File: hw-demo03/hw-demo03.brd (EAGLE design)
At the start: 83.5 x 63.5 mm, 41 parts, among them IC3 MCP2562T, IC4 STM32F042

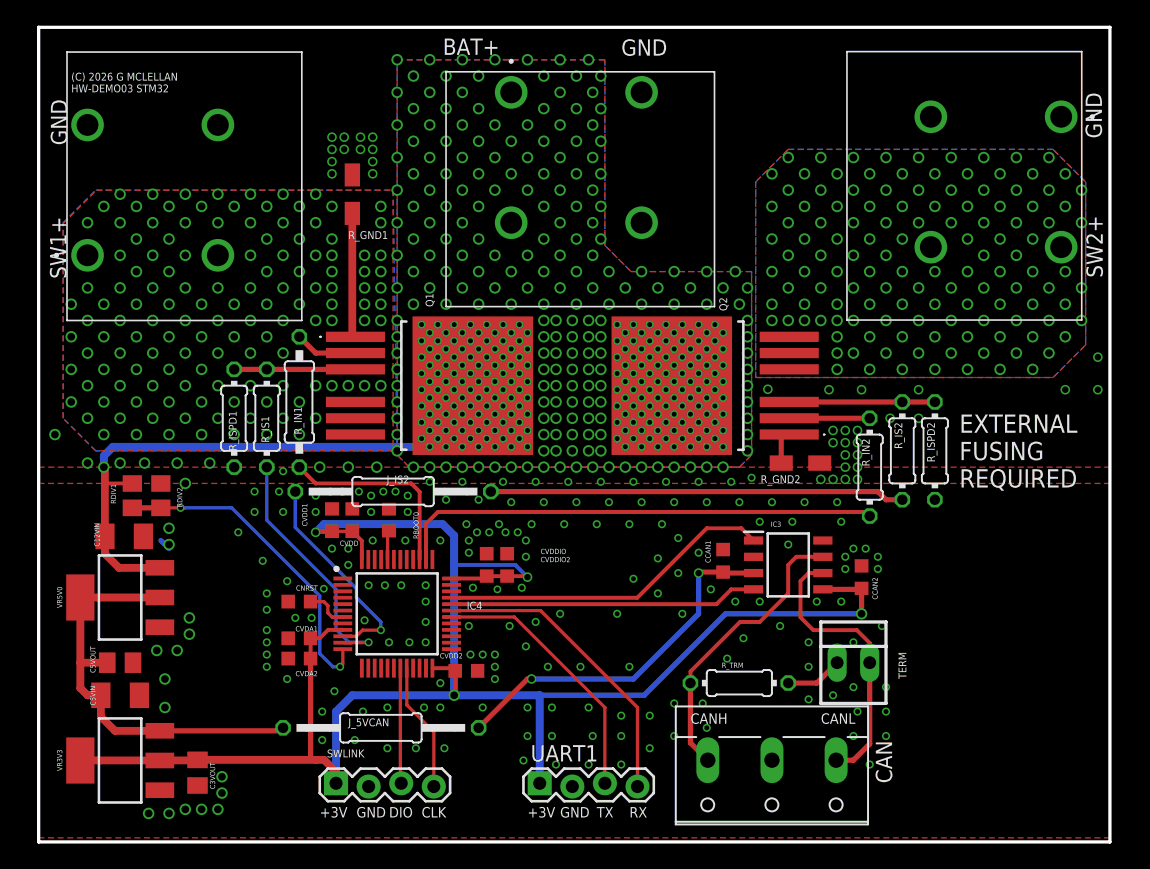
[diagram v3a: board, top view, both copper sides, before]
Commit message: add cap on voltage divider, more stitching
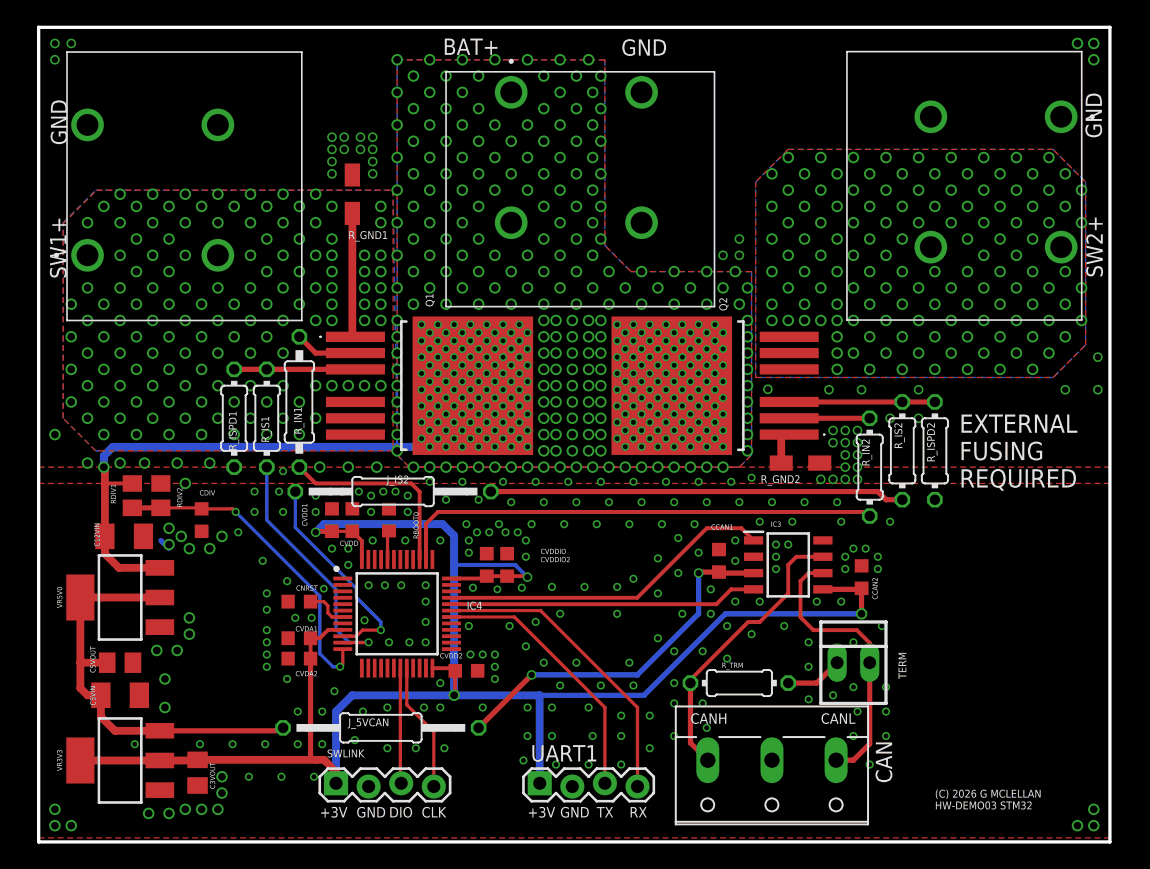
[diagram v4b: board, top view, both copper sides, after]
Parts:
- added CDIV: 100n, rcl:C0603K
- moved CCAN1 0.32 mm to (54.3, 21.9)
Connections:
- net ADC2: now also CDIV.1
- net GND: now also CDIV.2, IC3.8
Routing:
- net GND: vias 230 -> 277
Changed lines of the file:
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@@
 <text x="52.07" y="9.2075" size="0.8128" layer="25" font="vector" ratio="14">CANH</text>
 <text x="3.4925" y="54.2925" size="1.27" layer="25" font="vector" ratio="14" rot="R90">GND</text>
-<text x="3.81" y="58.42" size="0.6096" layer="25" font="vector" ratio="14">(C) 2026 G MCLELLAN
+<text x="71.12" y="2.54" size="0.6096" layer="25" font="vector" ratio="14">(C) 2026 G MCLELLAN
 HW-DEMO03 STM32</text>
 <text x="46.6725" y="61.2775" size="1.27" layer="25" font="vector" ratio="14">GND</text>
@@
 <attribute name="NAME" x="66.5153" y="7.9083" size="1.27" layer="25" font="vector" ratio="14" rot="R270"/>
 </element>
-<element name="CCAN1" library="rcl" package="C0603K" value="100n" x="54.61" y="21.9075" smashed="yes" rot="R90">
-<attribute name="NAME" x="53.6425" y="21.7425" size="0.4064" layer="25" font="vector" ratio="14" rot="R90"/>
+<element name="CCAN1" library="rcl" package="C0603K" value="100n" x="54.2925" y="21.9075" smashed="yes" rot="R90">
+<attribute name="NAME" x="55.41" y="24.75" size="0.4064" layer="25" font="vector" ratio="14" rot="R180"/>
 </element>
 <element name="CCAN2" library="rcl" package="C0603K" value="100n" x="65.405" y="20.6375" smashed="yes" rot="R90">
@@
 <element name="J_5VCAN" library="rcl" package="0207/15" value="000" x="27.94" y="8.89" smashed="yes" rot="R180">
 <attribute name="NAME" x="25.4" y="9.017" size="0.6096" layer="25" font="vector" ratio="14"/>
+</element>
+<element name="CDIV" library="rcl" package="C0603K" value="100n" x="13.97" y="25.0825" smashed="yes" rot="R270">
+<attribute name="NAME" x="13.805" y="27.0025" size="0.4064" layer="25" ratio="14"/>
 </element>
 </elements>
@@
 <contactref element="UART1" pad="2"/>
 <via x="32.5755" y="23.495" extent="1-16" drill="0.381"/>
-<via x="40.9575" y="13.6525" extent="1-16" drill="0.381"/>
+<via x="40.64" y="13.97" extent="1-16" drill="0.381"/>
 <via x="34.925" y="14.605" extent="1-16" drill="0.381"/>
 <via x="52.705" y="22.5425" extent="1-16" drill="0.381"/>
@@
 <via x="47.625" y="20.5105" extent="1-16" drill="0.381"/>
 <contactref element="SWLINK" pad="2"/>
-<via x="43.4975" y="13.6525" extent="1-16" drill="0.381"/>
+<via x="43.18" y="13.97" extent="1-16" drill="0.381"/>
 <via x="46.6725" y="6.0325" extent="1-16" drill="0.381"/>
-<via x="47.3075" y="13.6525" extent="1-16" drill="0.381"/>
+<via x="47.3075" y="13.97" extent="1-16" drill="0.381"/>
 <via x="54.9275" y="14.2875" extent="1-16" drill="0.381"/>
 <contactref element="BAT+" pad="2_2"/>
@@
 <vertex x="1.27" y="0.3175"/>
 </polygon>
-<via x="59.055" y="16.8275" extent="1-16" drill="0.381"/>
-<via x="56.1975" y="15.875" extent="1-16" drill="0.381"/>
+<via x="59.3725" y="16.8275" extent="1-16" drill="0.381"/>
+<via x="56.8325" y="16.1925" extent="1-16" drill="0.381"/>
 <contactref element="C12VIN" pad="2"/>
 <contactref element="VR5V0" pad="1"/>
@@
 <via x="24.3205" y="11.7475" extent="1-16" drill="0.381"/>
 <via x="23.368" y="10.16" extent="1-16" drill="0.381"/>
-<via x="23.368" y="7.9375" extent="1-16" drill="0.381"/>
+<via x="23.368" y="7.62" extent="1-16" drill="0.381"/>
 <via x="25.908" y="7.9375" extent="1-16" drill="0.381"/>
 <via x="26.543" y="10.16" extent="1-16" drill="0.381"/>
+<via x="46.355" y="19.8755" extent="1-16" drill="0.381"/>
+<via x="43.815" y="19.8755" extent="1-16" drill="0.381"/>
+<via x="41.275" y="19.8755" extent="1-16" drill="0.381"/>
+<via x="52.3875" y="24.765" extent="1-16" drill="0.381"/>
+<via x="2.54" y="1.27" extent="1-16" drill="0.6"/>
+<via x="2.54" y="2.54" extent="1-16" drill="0.6"/>
+<via x="3.81" y="1.27" extent="1-16" drill="0.6"/>
+<via x="83.5025" y="1.27" extent="1-16" drill="0.6"/>
+<via x="82.2325" y="1.27" extent="1-16" drill="0.6"/>
+<via x="83.5025" y="2.54" extent="1-16" drill="0.6"/>
+<via x="83.5025" y="62.23" extent="1-16" drill="0.6"/>
+<via x="83.5025" y="60.96" extent="1-16" drill="0.6"/>
+<via x="82.2325" y="62.23" extent="1-16" drill="0.6"/>
+<via x="3.81" y="62.23" extent="1-16" drill="0.5"/>
+<contactref element="CDIV" pad="2"/>
+<via x="12.3825" y="23.8125" extent="1-16" drill="0.6"/>
+<via x="15.5575" y="23.8125" extent="1-16" drill="0.6"/>
+<via x="13.0175" y="22.86" extent="1-16" drill="0.6"/>
+<via x="14.605" y="22.86" extent="1-16" drill="0.6"/>
+<via x="2.54" y="62.23" extent="1-16" drill="0.5"/>
+<via x="2.54" y="60.96" extent="1-16" drill="0.5"/>
+<via x="21.463" y="7.62" extent="1-16" drill="0.381"/>
+<via x="18.923" y="7.62" extent="1-16" drill="0.381"/>
+<via x="16.383" y="7.62" extent="1-16" drill="0.381"/>
+<via x="13.843" y="7.62" extent="1-16" drill="0.381"/>
+<via x="8.763" y="7.62" extent="1-16" drill="0.381"/>
+<via x="17.653" y="5.08" extent="1-16" drill="0.381"/>
+<via x="20.193" y="5.08" extent="1-16" drill="0.381"/>
+<via x="22.733" y="5.08" extent="1-16" drill="0.381"/>
+<via x="21.463" y="10.16" extent="1-16" drill="0.381"/>
+<via x="55.5625" y="21.9075" extent="1-16" drill="0.381"/>
+<via x="55.5625" y="23.495" extent="1-16" drill="0.381"/>
+<via x="58.7375" y="22.225" extent="1-16" drill="0.381"/>
+<via x="58.7375" y="23.1775" extent="1-16" drill="0.381"/>
+<via x="58.7375" y="21.2725" extent="1-16" drill="0.381"/>
+<contactref element="IC3" pad="8"/>
+<via x="55.88" y="45.72" extent="1-16" drill="0.5"/>
+<via x="55.88" y="46.99" extent="1-16" drill="0.5"/>
+<via x="54.61" y="45.72" extent="1-16" drill="0.5"/>
+<via x="67.6275" y="24.9555" extent="1-16" drill="0.381"/>
+<via x="41.91" y="12.192" extent="1-16" drill="0.381"/>
+<via x="45.085" y="12.192" extent="1-16" drill="0.381"/>
+<via x="47.625" y="12.192" extent="1-16" drill="0.381"/>
+<via x="53.6575" y="17.78" extent="1-16" drill="0.381"/>
+<via x="49.53" y="15.875" extent="1-16" drill="0.381"/>
+<via x="50.8" y="12.3825" extent="1-16" drill="0.381"/>
+<via x="54.9275" y="16.8275" extent="1-16" drill="0.381"/>
+<via x="50.8" y="14.859" extent="1-16" drill="0.381"/>
+<via x="53.0225" y="14.859" extent="1-16" drill="0.381"/>
 </signal>
 <signal name="CANH">
@@
 <wire x1="59.69" y1="21.59" x2="59.69" y2="19.3675" width="0.3048" layer="1"/>
 <wire x1="59.69" y1="19.3675" x2="57.4675" y2="17.145" width="0.3048" layer="1"/>
-<wire x1="57.4675" y1="17.145" x2="55.932553125" y2="17.145" width="0.3048" layer="1"/>
-<wire x1="55.932553125" y1="17.145" x2="52.07" y2="13.282446875" width="0.3048" layer="1"/>
-<wire x1="52.07" y1="13.282446875" x2="52.07" y2="12.3825" width="0.3048" layer="1"/>
+<wire x1="57.4675" y1="17.145" x2="56.567553125" y2="17.145" width="0.3048" layer="1"/>
+<wire x1="56.567553125" y1="17.145" x2="52.07" y2="12.647446875" width="0.3048" layer="1"/>
+<wire x1="52.07" y1="12.647446875" x2="52.07" y2="12.3825" width="0.3048" layer="1"/>
 <wire x1="53.42" y1="6.37" x2="52.07" y2="7.72" width="0.4064" layer="1"/>
 <wire x1="52.07" y1="7.72" x2="52.07" y2="12.3825" width="0.4064" layer="1"/>
@@
 <wire x1="24.765" y1="13.6525" x2="24.972" y2="13.8595" width="0.254" layer="1"/>
 <wire x1="24.972" y1="13.8595" x2="24.972" y2="15.03" width="0.254" layer="1"/>
-<wire x1="10.795" y1="26.0375" x2="12.33146875" y2="26.0375" width="0.254" layer="1"/>
-<via x="12.33146875" y="26.0375" extent="1-16" drill="0.381"/>
-<wire x1="12.33146875" y1="26.0375" x2="12.677753125" y2="26.0375" width="0.254" layer="16"/>
 <wire x1="23.1775" y1="14.67995" x2="23.1775" y2="19.172146875" width="0.254" layer="16"/>
-<wire x1="23.1775" y1="19.172146875" x2="16.312146875" y2="26.0375" width="0.254" layer="16"/>
-<wire x1="16.312146875" y1="26.0375" x2="12.33146875" y2="26.0375" width="0.254" layer="16"/>
+<wire x1="23.1775" y1="19.172146875" x2="16.629646875" y2="25.72" width="0.254" layer="16"/>
+<contactref element="CDIV" pad="1"/>
+<wire x1="10.795" y1="26.0375" x2="13.97" y2="26.0375" width="0.254" layer="1"/>
+<wire x1="13.97" y1="26.0375" x2="13.97" y2="25.9575" width="0.254" layer="1"/>
+<wire x1="13.97" y1="25.9575" x2="16.392146875" y2="25.9575" width="0.254" layer="1"/>
+<wire x1="16.392146875" y1="25.9575" x2="16.629646875" y2="25.72" width="0.254" layer="1"/>
+<via x="16.629646875" y="25.72" extent="1-16" drill="0.381"/>
 </signal>
 <signal name="BOOT0">
@@
 <contactref element="Q2" pad="1"/>
 <contactref element="R_GND2" pad="2"/>
-<wire x1="59.1435" y1="29.5275" x2="59.1435" y2="31.75" width="0.4064" layer="1"/>
+<wire x1="59.1435" y1="29.5275" x2="59.1435" y2="31.75" width="0.6096" layer="1"/>
 <wire x1="59.1435" y1="31.75" x2="59.765" y2="31.75" width="0.4064" layer="1"/>
 </signal>
@@
 <contactref element="CCAN1" pad="1"/>
 <contactref element="J_5VCAN" pad="1"/>
-<wire x1="54.61" y1="21.0325" x2="52.705" y2="21.0325" width="0.4064" layer="1"/>
+<wire x1="54.2925" y1="21.0325" x2="52.705" y2="21.0325" width="0.4064" layer="1"/>
 <wire x1="52.705" y1="21.0325" x2="52.705" y2="20.955" width="0.4064" layer="1"/>
 <via x="52.705" y="20.955" extent="1-16" drill="0.5"/>
 <wire x1="52.705" y1="20.955" x2="52.705" y2="17.78" width="0.4064" layer="16"/>
-<wire x1="52.705" y1="17.78" x2="47.625" y2="12.7" width="0.4064" layer="16"/>
-<wire x1="47.625" y1="12.7" x2="39.6875" y2="12.7" width="0.4064" layer="16"/>
-<wire x1="35.56" y1="8.89" x2="39.37" y2="12.7" width="0.4064" layer="1"/>
-<wire x1="39.37" y1="12.7" x2="39.6875" y2="12.7" width="0.4064" layer="1"/>
-<via x="39.6875" y="12.7" extent="1-16" drill="0.5"/>
+<wire x1="52.705" y1="17.78" x2="47.9425" y2="13.0175" width="0.4064" layer="16"/>
+<wire x1="47.9425" y1="13.0175" x2="39.6875" y2="13.0175" width="0.4064" layer="16"/>
+<wire x1="35.56" y1="8.89" x2="39.6875" y2="13.0175" width="0.4064" layer="1"/>
+<via x="39.6875" y="13.0175" extent="1-16" drill="0.5"/>
 <wire x1="56.99" y1="20.955" x2="54.6875" y2="20.955" width="0.4064" layer="1"/>
-<wire x1="54.6875" y1="20.955" x2="54.61" y2="21.0325" width="0.4064" layer="1"/>
+<wire x1="54.6875" y1="20.955" x2="54.2925" y2="21.0325" width="0.4064" layer="1"/>
 </signal>
 </signals>

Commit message: pretty happy with the layout
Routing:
- net GND: vias 277 -> 279
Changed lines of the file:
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@@
 </element>
 <element name="R_IN1" library="rcl" package="0207/10" value="4K7" x="21.59" y="34.29" smashed="yes" rot="R90">
-<attribute name="NAME" x="21.7805" y="31.75" size="0.6096" layer="25" font="vector" ratio="14" rot="R90"/>
+<attribute name="NAME" x="25.0825" y="30.988" size="0.6096" layer="25" font="vector" ratio="14" rot="R180"/>
 </element>
 <element name="BAT+" library="VP0265840000G" package="AMPHENOL_VP0265840000G" value="" x="43.18" y="53.34" smashed="yes">
@@
 </element>
 <element name="R_ISPD1" library="rcl" package="0204/7" value="1K0" x="16.51" y="33.02" smashed="yes" rot="R90">
-<attribute name="NAME" x="16.7005" y="30.48" size="0.6096" layer="25" ratio="10" rot="R90"/>
+<attribute name="NAME" x="17.78" y="30.988" size="0.6096" layer="25" ratio="10" rot="R180"/>
 </element>
 <element name="R_IS1" library="rcl" package="0204/7" value="10K" x="19.05" y="33.02" smashed="yes" rot="R270">
-<attribute name="NAME" x="19.2405" y="31.115" size="0.6096" layer="25" ratio="10" rot="R90"/>
+<attribute name="NAME" x="20.6375" y="30.988" size="0.6096" layer="25" ratio="10" rot="R180"/>
 </element>
 <element name="R_GND1" library="rcl" package="R1206W" value="0R0" x="25.7175" y="50.4825" smashed="yes" rot="R270">
@@
 <via x="16.8275" y="24.13" extent="1-16" drill="0.381"/>
 <via x="18.7325" y="21.9075" extent="1-16" drill="0.381"/>
-<via x="33.02" y="26.67" extent="1-16" drill="0.381"/>
 <via x="34.6075" y="24.765" extent="1-16" drill="0.381"/>
 <via x="37.1475" y="24.765" extent="1-16" drill="0.381"/>
@@
 <via x="47.3075" y="24.765" extent="1-16" drill="0.381"/>
 <via x="49.8475" y="24.765" extent="1-16" drill="0.381"/>
-<via x="35.56" y="26.67" extent="1-16" drill="0.381"/>
 <via x="38.1" y="26.4795" extent="1-16" drill="0.381"/>
 <via x="40.64" y="26.4795" extent="1-16" drill="0.381"/>
@@
 <via x="28.448" y="7.3025" extent="1-16" drill="0.381"/>
 <via x="28.448" y="10.4775" extent="1-16" drill="0.381"/>
-<via x="24.3205" y="11.7475" extent="1-16" drill="0.381"/>
+<via x="24.9555" y="12.065" extent="1-16" drill="0.381"/>
 <via x="23.368" y="10.16" extent="1-16" drill="0.381"/>
 <via x="23.368" y="7.62" extent="1-16" drill="0.381"/>
@@
 <via x="50.8" y="14.859" extent="1-16" drill="0.381"/>
 <via x="53.0225" y="14.859" extent="1-16" drill="0.381"/>
+<via x="35.56" y="26.4795" extent="1-16" drill="0.381"/>
+<via x="33.655" y="26.4795" extent="1-16" drill="0.381"/>
+<via x="31.75" y="26.4795" extent="1-16" drill="0.381"/>
+<via x="45.72" y="13.97" extent="1-16" drill="0.381"/>
 </signal>
 <signal name="CANH">

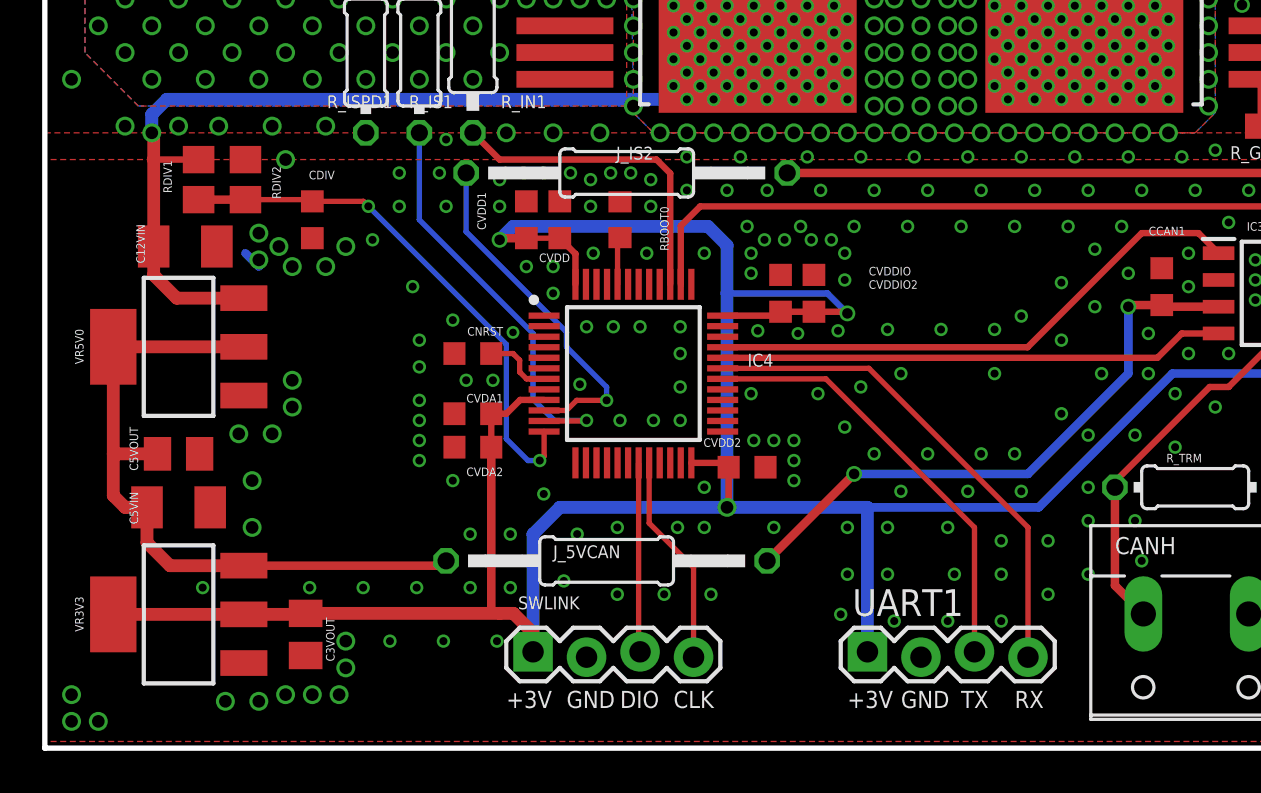
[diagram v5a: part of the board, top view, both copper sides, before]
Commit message: added inexpensive 5v smps module to replace 5v linear
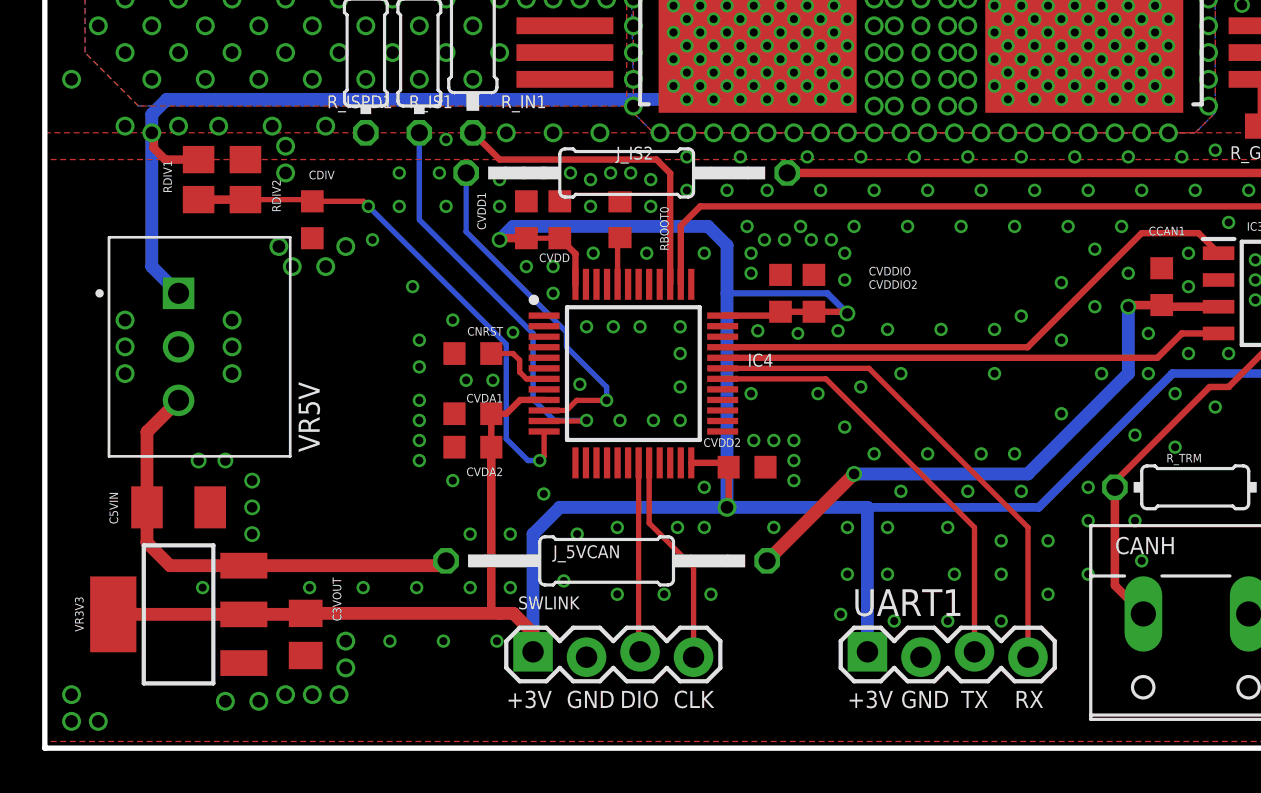
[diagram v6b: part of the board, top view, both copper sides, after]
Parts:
- removed C12VIN: 1u, rcl:C1206K
- removed C5VOUT: 1u, rcl:C0805K
- removed VR5V0: (no value), SparkFun-PowerIC:SOT223
- added VR5V: (no value), OKI-78SR-5_1.5-W36-C:CONV_OKI-78SR-5/1.5-W36-C
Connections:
- net +12V: now also VR5V.1; no longer C12VIN.1, VR5V0.3
- net +5V: now also VR5V.3; no longer C5VOUT.1, VR5V0.2, VR5V0.4
- net GND: now also VR5V.2; no longer C12VIN.2, C5VOUT.2, VR5V0.1
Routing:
- net +5V: track 33.9 -> 22.1 mm
- net +12V: track 40.3 -> 37.9 mm
- net GND: track 0.90 -> 0.00 mm, vias 279 -> 282
